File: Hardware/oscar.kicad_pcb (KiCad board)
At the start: 4 copper layers, 71 x 110 mm, 49 parts, among them J1 SWD_Header, J2 ChannelA_In, J3 ChannelB_In, J4 ChannelC_In, J5 ChA_Buff_Out, J6 ChB_Buff_Out, J7 ChC_Buff_Out, J8 MIDI_In, J9 Eurorack_10_pin_power, SW3 SW_Push, U1 STM32F446RETx, U2 ILI9341_SPI_Daughterboard, U3 MCP6004, U4 TL074, U5 LM1117-3.3, Y1 Crystal

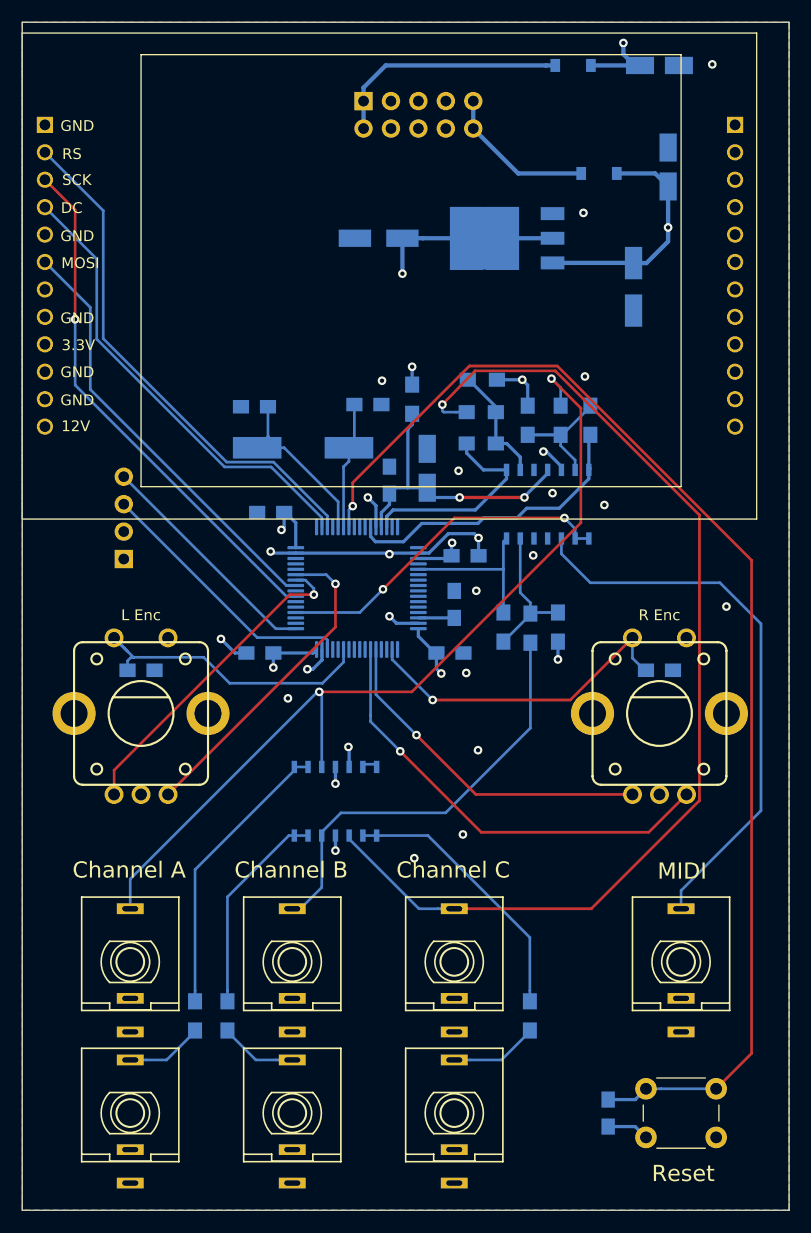
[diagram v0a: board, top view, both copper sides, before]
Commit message: Reorganised and relocated reposistory
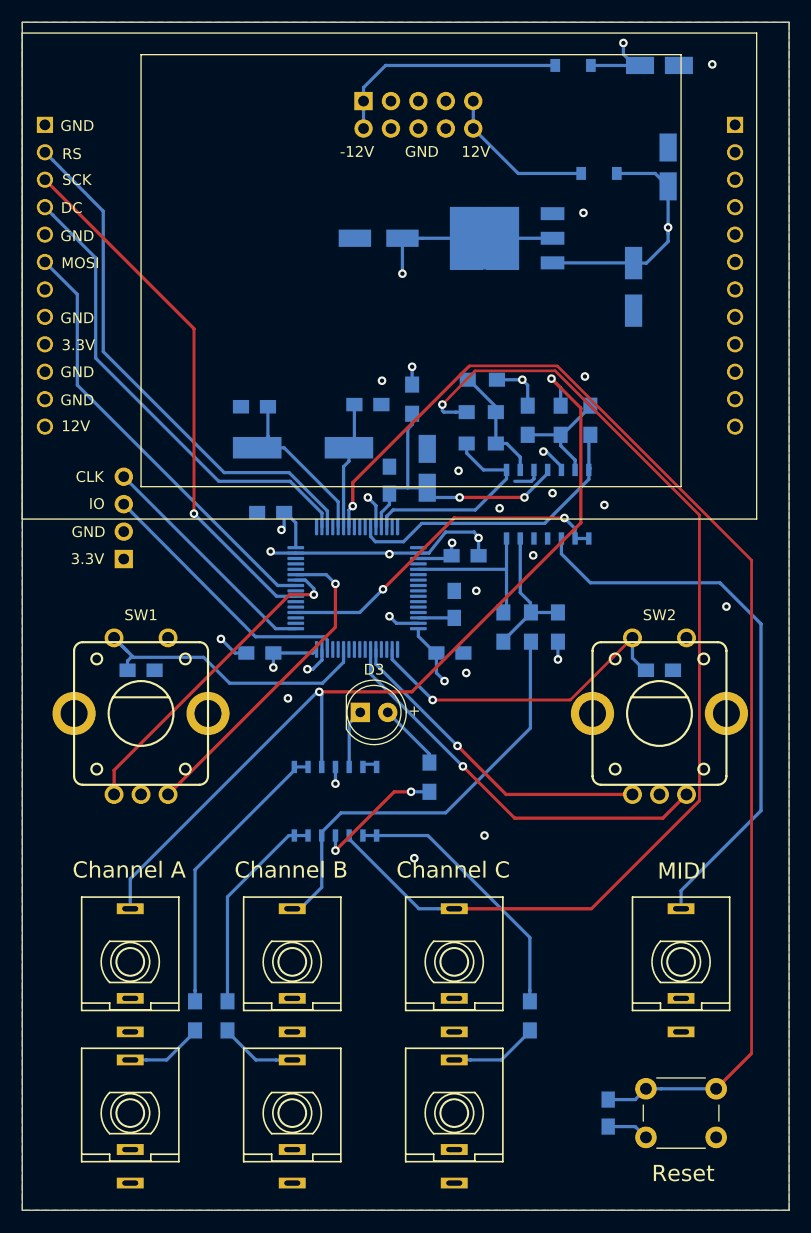
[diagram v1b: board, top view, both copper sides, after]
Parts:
- added D3: LED, LEDs:LED_D5.0mm, F.Cu at (156.3, 113.9)
- added R13: 680, Resistors_SMD:R_0805_HandSoldering, B.Cu at (162.7, 119.9)
- SW1: renamed from L Enc
- SW2: renamed from R Enc
- moved R4 0.11 mm to (172.1, 106.0)
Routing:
- net VCC: track 23.3 -> 34.3 mm, vias 2 -> 3
- net GND: track 41.9 -> 48.5 mm, vias 24 -> 23
- net Net-(D3-Pad2): track 0.00 -> 6.25 mm
- net R_ENC_DN: track 41.6 -> 38.0 mm
- net R_ENC_UP: track 31.8 -> 30.1 mm
- net LCD_DC: track 42.7 -> 44.1 mm
- net LCD_RESET: track 48.1 -> 49.0 mm
- net +3V3: track 39.3 -> 40.1 mm
- net LCD_SCK: track 48.7 -> 49.2 mm
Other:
- board text added: "+"
- board text added: "3V3"
- board text added: "CLK"
- board text added: "IO"

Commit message: Increased oscillator max voltage from 8V to 12V; fixes to FFT menu (allows channel select in config)
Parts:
- R7, R8, R9: value 15k -> 14k
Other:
- board text added: "Oscar v3 Mountjoy Modular"
- board text removed: "Oscar v2 Mountjoy Modular"
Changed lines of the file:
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@@
   )
   (setup
-    (last_trace_width 0.3)
+    (last_trace_width 0.25)
     (user_trace_width 0.25)
     (user_trace_width 0.3)
@@
       (effects (font (size 1 1) (thickness 0.15)) (justify mirror))
     )
-    (fp_text value 15k (at -0.5 3.3) (layer B.SilkS)
+    (fp_text value 14k (at -0.5 3.3) (layer B.SilkS)
       (effects (font (size 1 1) (thickness 0.15)) (justify mirror))
     )
@@
       (effects (font (size 1 1) (thickness 0.15)) (justify mirror))
     )
-    (fp_text value 15k (at -0.8 2.6 180) (layer B.SilkS)
+    (fp_text value 14k (at -0.8 2.6 180) (layer B.SilkS)
       (effects (font (size 1 1) (thickness 0.15)) (justify mirror))
     )
@@
       (effects (font (size 1 1) (thickness 0.15)) (justify mirror))
     )
-    (fp_text value 15k (at 4 0.075 270) (layer B.SilkS)
+    (fp_text value 14k (at 4 0.075 270) (layer B.SilkS)
       (effects (font (size 1 1) (thickness 0.15)) (justify mirror))
     )
@@
     (effects (font (size 1 1) (thickness 0.15)))
   )
-  (gr_text "Oscar v2\n\nMountjoy\nModular" (at 145.7 58.5) (layer B.SilkS)
+  (gr_text "Oscar v3\n\nMountjoy\nModular" (at 145.7 58.5) (layer B.SilkS)
     (effects (font (size 1.5 1.5) (thickness 0.3)) (justify left mirror))
   )

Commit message: Added readme and graphics
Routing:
- added copper zone on In2.Cu, net +3V3
- added copper zone on In1.Cu, net GND
- added copper zone on In2.Cu, net VCC
- added copper zone on In2.Cu, net VEE
- removed copper zone on PWR, net +3V3
- removed copper zone on GND, net GND
- removed copper zone on PWR, net VCC
- removed copper zone on PWR, net VEE
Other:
- net class Default removed
